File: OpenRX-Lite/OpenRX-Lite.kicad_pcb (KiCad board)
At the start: 6 copper layers, 8.8 x 13 mm, 37 parts, among them U1 ESP32-C3FH4, U2 TLV75533PDQNR, U3 SX1281IMLTRT, X1 CJ17-400001010B20

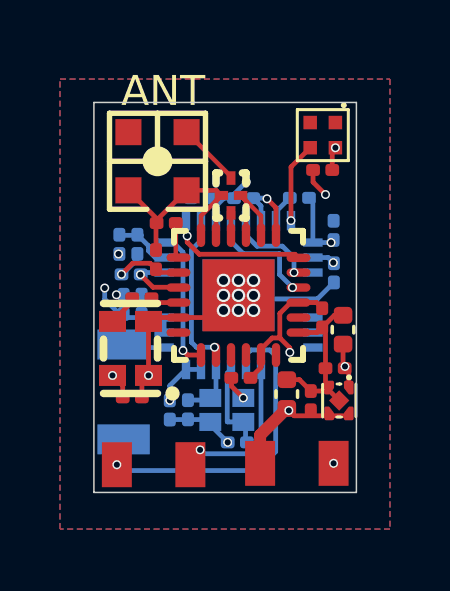
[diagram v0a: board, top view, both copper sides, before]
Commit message: Update schematics: Mono RF rewiring, SKY13414 port mapping, shared libs
Mono: disconnect IPD TX_LP (unused by ELRS), route TX_HP→RF3, RX→RF1,
RFX2401C ANT→RF4. Matches BetaFPV SuperX topology.

Co-Authored-By: Claude Opus 4.6 (1M context) <noreply@anthropic.com>
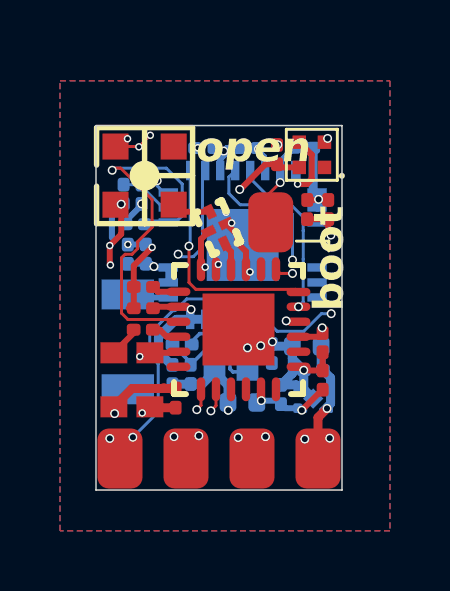
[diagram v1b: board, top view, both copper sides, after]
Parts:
- added L1: 24nH, Inductor_SMD:L_0201_0603Metric, B.Cu at (182.1, 97.8)
- added TP5: GND, OpenRX-Shared:SolderPad_1.2x2.0mm, F.Cu at (185.0, 93.8)
- C10: renamed from C9; moved to B.Cu
- C11: renamed from C4; moved to F.Cu
- C15: renamed from C10; moved to B.Cu
- C16: renamed from C11; moved to B.Cu
- C8: renamed from C12; moved to B.Cu
- C9: renamed from C3; moved to F.Cu
- FL1: renamed from USB1; value DEA102700LT-6307A2 -> 2450FM07D0034
- TP1, TP2, TP3, TP4: footprint OpenRX-Shared:SolderPad_1.0x1.5mm -> OpenRX-Shared:SolderPad_1.2x2.0mm
- U2: moved to B.Cu
- moved C16 4.14 mm to (184.1, 99.8), turned to 180 degrees
- moved C3 3.18 mm to (185.1, 98.1), turned to 90 degrees
- moved C17 2.97 mm to (186.8, 97.8), turned to -90 degrees
- moved TP4 2.72 mm to (184.4, 101.7), turned to 180 degrees
- moved C20 2.26 mm to (180.8, 95.9)
- moved C9 2.12 mm to (186.9, 93.3)
- moved C18 2.08 mm to (186.8, 99.0), turned to 90 degrees
- moved C15 2.01 mm to (185.4, 99.5), turned to 90 degrees
- moved TP3 1.94 mm to (186.6, 101.7), turned to 180 degrees
- moved C8 1.73 mm to (186.2, 97.9), turned to 180 degrees
- moved C2 1.68 mm to (180.1, 92.8)
- moved C5 1.68 mm to (180.9, 94.8)
- moved U1 1.68 mm to (184.1, 94.5)
- moved AE1 1.68 mm to (180.3, 97.8)
- moved C12 1.68 mm to (182.8, 91.3)
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- renumbered C6 to C1, C5 to C12, C17 to C14, C15 to C17, C14 to C18, C18 to C19, C8 to C2, C16 to C20, C7 to C3, C19 to C4, C1 to C5, C2 to C6, C20 to C7, R4 to R2, R2 to R3, R3 to R4
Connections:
- C1 pad 1: /ESP32-C3 + SX1281 Core/XTAL_P -> Net-(C1-Pad1)
- X1 pad 1: /ESP32-C3 + SX1281 Core/XTAL_P -> Net-(C1-Pad1)
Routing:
- net /ESP32-C3 + SX1281 Core/RST: track 2.25 -> 13.2 mm
- net GND: track 31.6 -> 38.0 mm, vias 16 -> 28
- net Net-(U1-U0RXD): track 4.76 -> 10.7 mm, vias 1 -> 3
- net /ESP32-C3 + SX1281 Core/BUSY: track 4.70 -> 9.55 mm, vias 1 -> 2
- net /ESP32-C3 + SX1281 Core/NSS: track 2.66 -> 7.45 mm, vias 1 -> 2
- net /ESP32-C3 + SX1281 Core/DIO1: track 5.30 -> 10.0 mm, vias 1 -> 2
- net /ESP32-C3 + SX1281 Core/MISO: track 3.98 -> 7.04 mm, vias 1 -> 2
- net /ESP32-C3 + SX1281 Core/SCK: track 4.66 -> 7.53 mm
- net /ESP32-C3 + SX1281 Core/MOSI: track 3.04 -> 5.63 mm
- net +5V: track 14.8 -> 16.9 mm, vias 2 -> 4
- net Net-(C1-Pad1): track 0.00 -> 1.95 mm
- net /ESP32-C3 + SX1281 Core/CHIP_BOOT: track 0.95 -> 2.76 mm, vias 0 -> 1
- net +3V3: track 21.1 -> 19.8 mm
- net Net-(FL1-OUT): track 2.14 -> 1.34 mm
- net Net-(U1-U0TXD): track 10.5 -> 9.84 mm, vias 1 -> 2
- added copper zone on In3.Cu, net +3V3
- added copper zone on In1.Cu, net GND
- added copper zone on In4.Cu, net GND
- removed copper zone on In1.Cu, net +3V3
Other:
- board size 8.8 x 13 mm -> 8.2 x 12.2 mm
- board text added: "5v"
- board text added: "GND"
- board text added: "RX"
- board text added: "TX"
- board text added: "boot"
- board text added: "open"
